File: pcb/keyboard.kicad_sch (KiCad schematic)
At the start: 61 parts, among them J1 Tag-Connect TC2030, J1 USB4510-03-1-A, J4 Battery (JST_S2B-PH-K-S), Q2 2N7002, SW1 PWR, U1 SRV05-4, U3 BQ24075, U3 BT840, Y1 ECS-.327-9-34B-TR

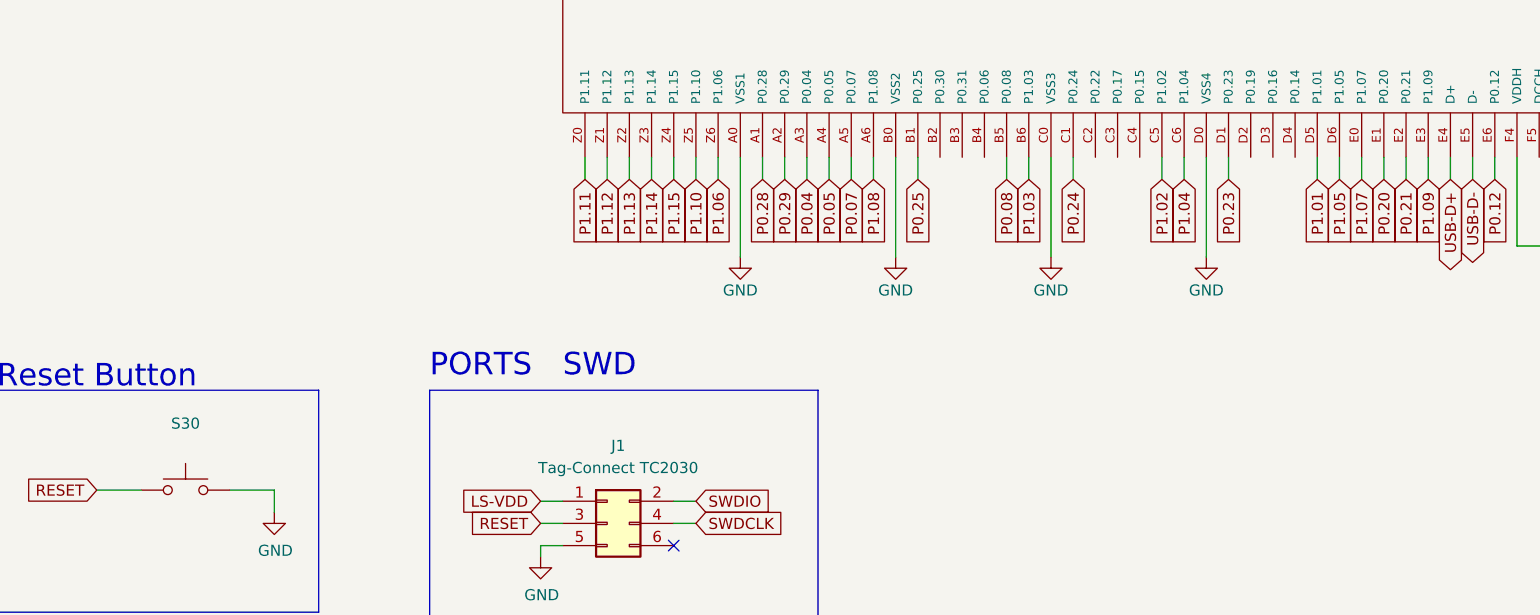
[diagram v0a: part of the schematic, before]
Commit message: #1 Select reset switch and LED
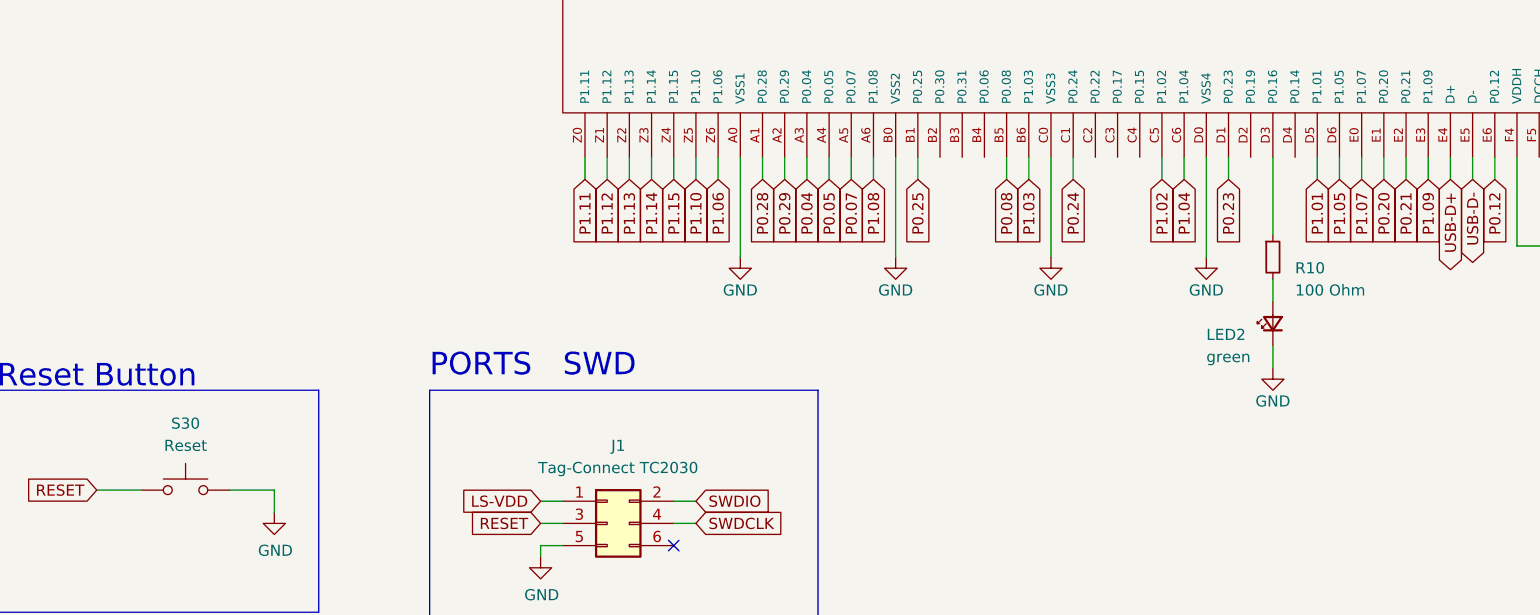
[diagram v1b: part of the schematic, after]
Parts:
- added LED2: green, LED_SMD:LED_0603_1608Metric, symbol Device:LED_Small
- added R10: 100 Ohm, Resistor_SMD:R_0603_1608Metric, symbol Device:R_Small
- S30: value ~ -> Reset; footprint (none) -> Button_Switch_SMD:SW_SPST_B3S-1000; Digikey (none) -> https://www.digikey.fr/short/qt5jdm9z; Mfr Part Number (none) -> B3S-1000
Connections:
- net GND: now also LED2.1 (K)
- net at U3.D3 (P0.16): now also R10.1
- new net: LED2.2 (A), R10.2
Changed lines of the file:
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@@
     (stroke (width 0) (type default))
   )
+  (wire (pts (xy 341.63 243.84) (xy 341.63 246.38))
+    (stroke (width 0) (type default))
+  )
   (wire (pts (xy 280.67 222.25) (xy 280.67 233.68))
     (stroke (width 0) (type default))
@@
     (stroke (width 0) (type default))
   )
+  (wire (pts (xy 341.63 236.22) (xy 341.63 238.76))
+    (stroke (width 0) (type default))
+  )
   (wire (pts (xy 207.01 260.35) (xy 212.09 260.35))
     (stroke (width 0) (type default))
@@
     (stroke (width 0) (type solid))
   )
+  (wire (pts (xy 341.63 222.25) (xy 341.63 231.14))
+    (stroke (width 0) (type default))
+  )
   (wire (pts (xy 247.65 180.34) (xy 247.65 182.88))
     (stroke (width 0) (type default))
@@
     )
   )
+  (symbol (lib_id "power:GND") (at 341.63 246.38 0) (unit 1)
+    (in_bom yes) (on_board yes) (dnp no)
+    (property "Reference" "#PWR010" (at 341.63 252.73 0)
+      (effects (font (size 1.27 1.27)) hide)
+    )
+    (property "Value" "GND" (at 341.63 250.19 0)
+      (effects (font (size 1.27 1.27)))
+    )
+    (property "Footprint" "" (at 341.63 246.38 0)
+      (effects (font (size 1.27 1.27)) hide)
+    )
+    (property "Datasheet" "" (at 341.63 246.38 0)
+      (effects (font (size 1.27 1.27)) hide)
+    )
+    (pin "1")
+    (instances
+      (project "designguide-schematic"
+        (path "/c2a65ddb-3915-4293-98a9-444287fe2a3d"
+          (reference "#PWR010") (unit 1)
+        )
+      )
+      (project "keyboard"
+        (path "/cf0c78e1-ddbc-47c3-b3dc-2a4f1ccfd0ad"
+          (reference "#PWR060") (unit 1)
+        )
+      )
+    )
+  )
   (symbol (lib_id "power:GND") (at 102.87 49.53 0) (unit 1)
     (in_bom yes) (on_board yes) (dnp no)
@@
     )
   )
+  (symbol (lib_id "Device:LED_Small") (at 341.63 241.3 90) (unit 1)
+    (in_bom yes) (on_board yes) (dnp no)
+    (property "Reference" "LED2" (at 334.01 242.57 90)
+      (effects (font (size 1.27 1.27)) (justify right))
+    )
+    (property "Value" "green" (at 334.01 245.11 90)
+      (effects (font (size 1.27 1.27)) (justify right))
+    )
+    (property "Footprint" "LED_SMD:LED_0603_1608Metric" (at 341.63 241.3 90)
+      (effects (font (size 1.27 1.27)) hide)
+    )
+    (property "Datasheet" "~" (at 341.63 241.3 90)
+      (effects (font (size 1.27 1.27)) hide)
+    )
+    (property "Digikey" "" (at 341.63 241.3 0)
+      (effects (font (size 1.27 1.27)) hide)
+    )
+    (property "Mfr Part Number" "" (at 341.63 241.3 0)
+      (effects (font (size 1.27 1.27)) hide)
+    )
+    (pin "1")
+    (pin "2")
+    (instances
+      (project "designguide-schematic"
+        (path "/c2a65ddb-3915-4293-98a9-444287fe2a3d"
+          (reference "LED2") (unit 1)
+        )
+      )
+      (project "keyboard"
+        (path "/cf0c78e1-ddbc-47c3-b3dc-2a4f1ccfd0ad"
+          (reference "LED2") (unit 1)
+        )
+      )
+    )
+  )
   (symbol (lib_id "Device:L_Small") (at 49.53 262.89 90) (unit 1)
     (in_bom yes) (on_board yes) (dnp no) (fields_autoplaced)
@@
     )
   )
+  (symbol (lib_id "Device:R_Small") (at 341.63 233.68 0) (unit 1)
+    (in_bom yes) (on_board yes) (dnp no)
+    (property "Reference" "R10" (at 344.17 234.95 0)
+      (effects (font (size 1.27 1.27)) (justify left))
+    )
+    (property "Value" "100 Ohm" (at 344.17 237.49 0)
+      (effects (font (size 1.27 1.27)) (justify left))
+    )
+    (property "Footprint" "Resistor_SMD:R_0603_1608Metric" (at 341.63 233.68 0)
+      (effects (font (size 1.27 1.27)) hide)
+    )
+    (property "Datasheet" "~" (at 341.63 233.68 0)
+      (effects (font (size 1.27 1.27)) hide)
+    )
+    (property "Digikey" "" (at 341.63 233.68 0)
+      (effects (font (size 1.27 1.27)) hide)
+    )
+    (property "Mfr Part Number" "" (at 341.63 233.68 0)
+      (effects (font (size 1.27 1.27)) hide)
+    )
+    (pin "1")
+    (pin "2")
+    (instances
+      (project "designguide-schematic"
+        (path "/c2a65ddb-3915-4293-98a9-444287fe2a3d"
+          (reference "R10") (unit 1)
+        )
+      )
+      (project "keyboard"
+        (path "/cf0c78e1-ddbc-47c3-b3dc-2a4f1ccfd0ad"
+          (reference "R12") (unit 1)
+        )
+      )
+    )
+  )
   (symbol (lib_id "Switch:SW_Push") (at 217.17 260.35 0) (unit 1)
     (in_bom yes) (on_board yes) (dnp no) (fields_autoplaced)
@@
       (effects (font (size 1.27 1.27)))
     )
-    (property "Value" "~" (at 217.17 255.27 0)
+    (property "Value" "Reset" (at 217.17 255.27 0)
       (effects (font (size 1.27 1.27)))
     )
-    (property "Footprint" "" (at 217.17 255.27 0)
+    (property "Footprint" "Button_Switch_SMD:SW_SPST_B3S-1000" (at 217.17 255.27 0)
       (effects (font (size 1.27 1.27)) hide)
     )
-    (property "Datasheet" "~" (at 217.17 255.27 0)
+    (property "Datasheet" "https://omronfs.omron.com/en_US/ecb/products/pdf/en-b3s.pdf" (at 217.17 255.27 0)
       (effects (font (size 1.27 1.27)) hide)
     )
-    (property "Digikey" "" (at 217.17 260.35 0)
+    (property "Digikey" "https://www.digikey.fr/short/qt5jdm9z" (at 217.17 260.35 0)
       (effects (font (size 1.27 1.27)) hide)
     )
-    (property "Mfr Part Number" "" (at 217.17 260.35 0)
+    (property "Mfr Part Number" "B3S-1000" (at 217.17 260.35 0)
       (effects (font (size 1.27 1.27)) hide)
     )
